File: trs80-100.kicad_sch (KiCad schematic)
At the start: 120 parts, among them CN2 A-7224, CN3 TCS-4480, CN4 TCS-4490, CN6 RS232C, J1 Adapter Jack CN9, M27 4011, M28 4013, SW3 SLB-22BP-03, SW4 Reset Switch, SW5 SSP32201, T10 2SC2603, T11 2SC2603, T13 2SC2603(E), T14 2SC2603(E), T15 2SC2603(E), T16 2SC2603(E), T17 2SC2603(E), T18 2SC2603, T19 2SA1115, T20 2SC2603, T21 2SC2603(E), T22 2SC2603(E), T25 2SC2603, T27 2SC2603, T28 2SA1115, T9 2SC2603

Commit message: Progress BCR, CMT section.
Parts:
- added C63: 100n, symbol Device:C
- added C64, C67: 47n, symbol Device:C
- added D17, D5, D6, D7: 1S2076, symbol Device:D
- added M30: TL064, symbol Amplifier_Operational:TL064
- added M34: 4584, symbol trs80-100:4584
- added R131, R52: 1k, symbol Device:R
- added R132: 150k, symbol Device:R
- added R136, R93: 68k, symbol Device:R
- added R50, R55: 3.3k, symbol Device:R
- added R51: 2.2k, symbol Device:R
- added R53: 100k, symbol Device:R
- added R54: 12k, symbol Device:R
- added R62, R67, R71, R72: 33k, symbol Device:R
- added R95: 100, symbol Device:R
- added RY1: FBR211CD005-M, symbol trs80-100:FBR211CD005-M
- added T6: 2SC2603, Package_TO_SOT_THT:TO-92_Inline, symbol Transistor_BJT:2N3904
- renumbered R52 to R152, Rqq to R999
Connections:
- net GNDPWR: now also C64.1, C67.2, D5.2 (A), D6.1 (K), D7.2 (A), M34.7 (GND), R131.2, R53.2, R55.2, R93.2, T6.1 (E)
- net VDD: now also C67.1, M30.4 (V+), M34.14 (VCC), R136.1, R62.2, R67.2, R71.2
- net VEE: now also M30.11 (V-)
- net VR: now also D17.1 (K), RY1.5
- net at CN2.2 (RxD), R70.1: now also M34.9
- net at CN3.1 (REM1): now also RY1.4
- net at CN3.3 (REM2): now also RY1.6
- net at CN3.4 (RxC): now also R95.1
- net at CN3.5 (TxC): now also R54.1, R55.1
- new net: M30.10 (+), R131.1, R132.1, R136.2
- new net: M30.8, R132.2, R72.1
- new net: D5.1 (K), D6.2 (A), R52.1, R53.1, R95.2
- new net: R50.1, R93.1, T6.2 (B)
- new net: M34.4, R50.2
- new net: C63.2, M34.12, R71.1
- new net: D7.1 (K), M34.11, R72.2
- new net: M30.9 (-), R52.2
- new net: D17.2 (A), RY1.2, T6.3 (C)
- new net: C64.2, R51.1, R54.2
- new net: C63.1, R51.2
- new net: M34.10, R62.1
- new net ~{REMOTE}: M34.3, R67.1
- no-connect marks 1 -> 8
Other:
- moved on the sheet: CN3, CN4

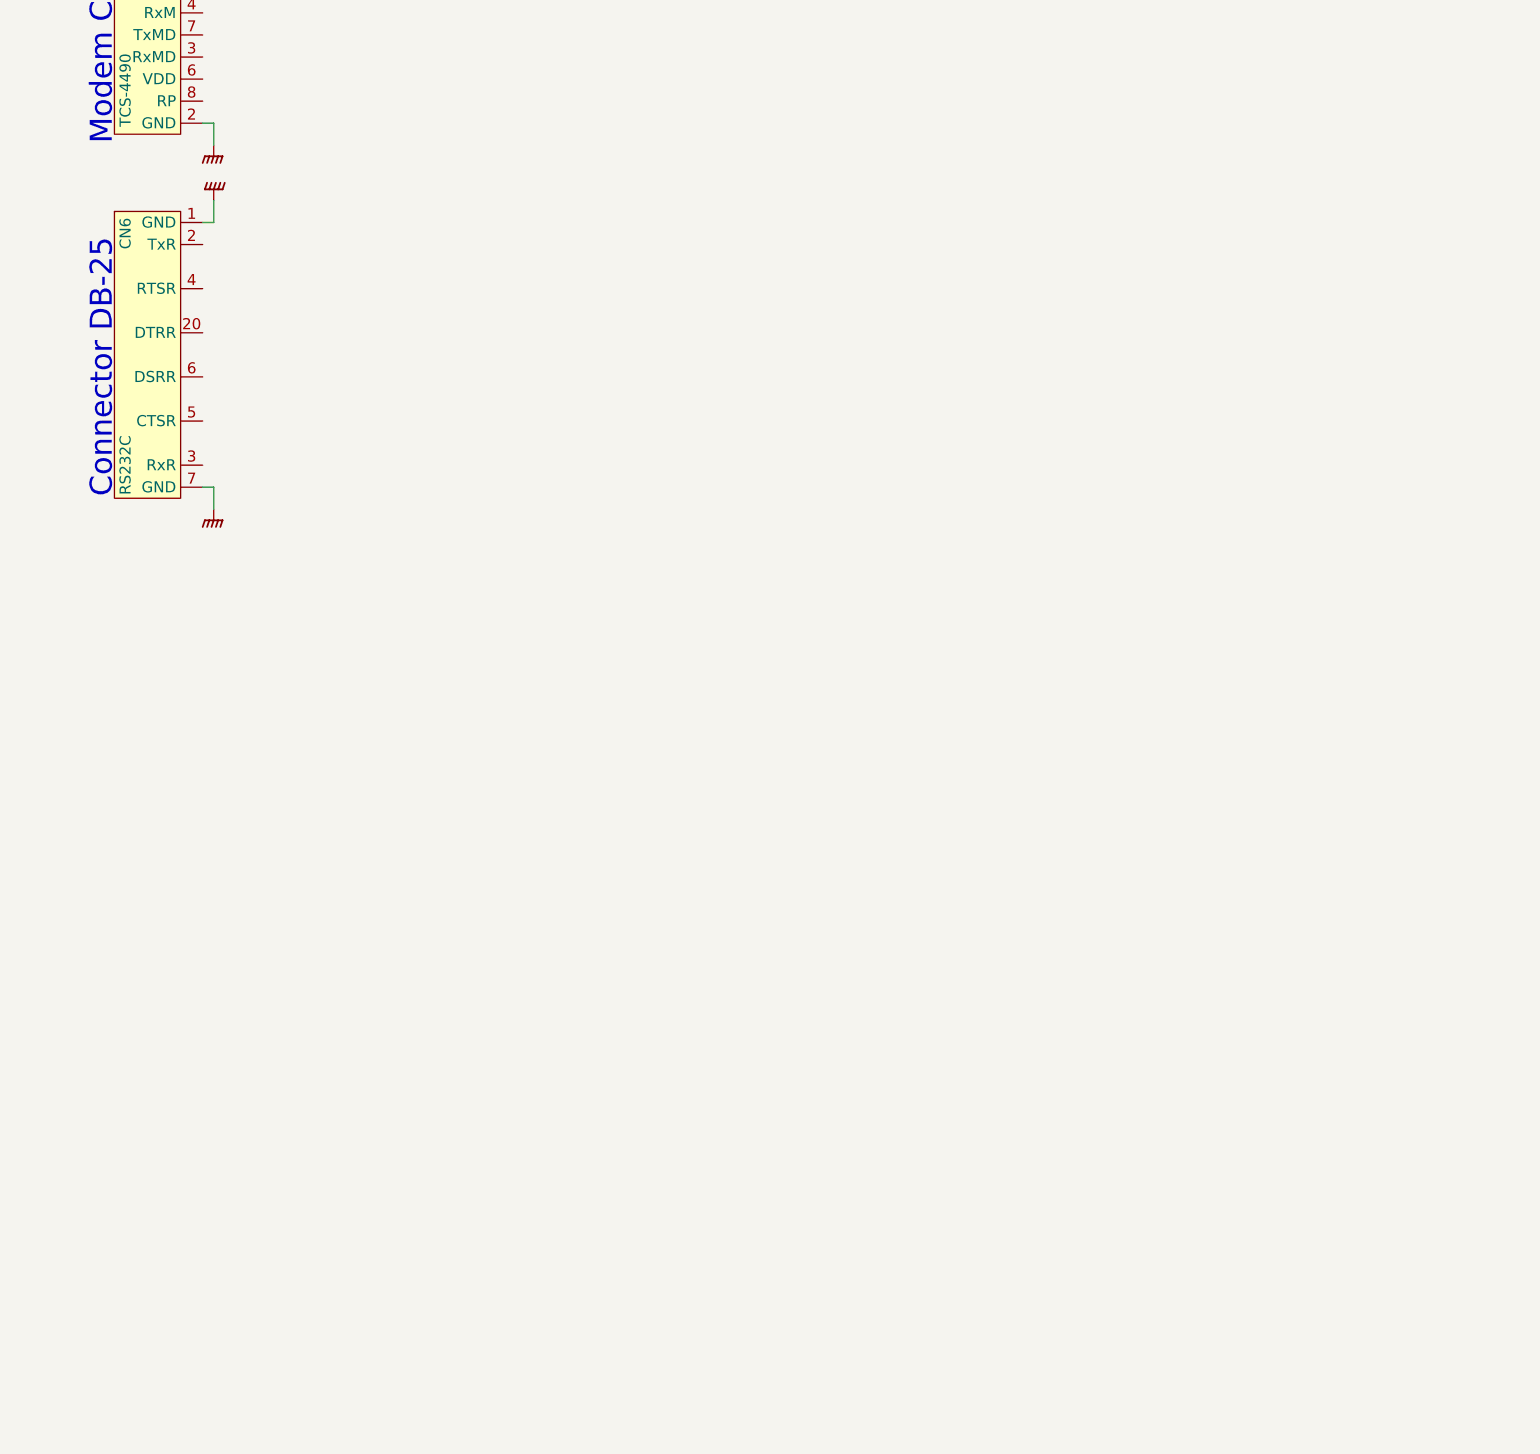
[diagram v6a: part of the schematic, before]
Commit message: Progress RS232 interface.
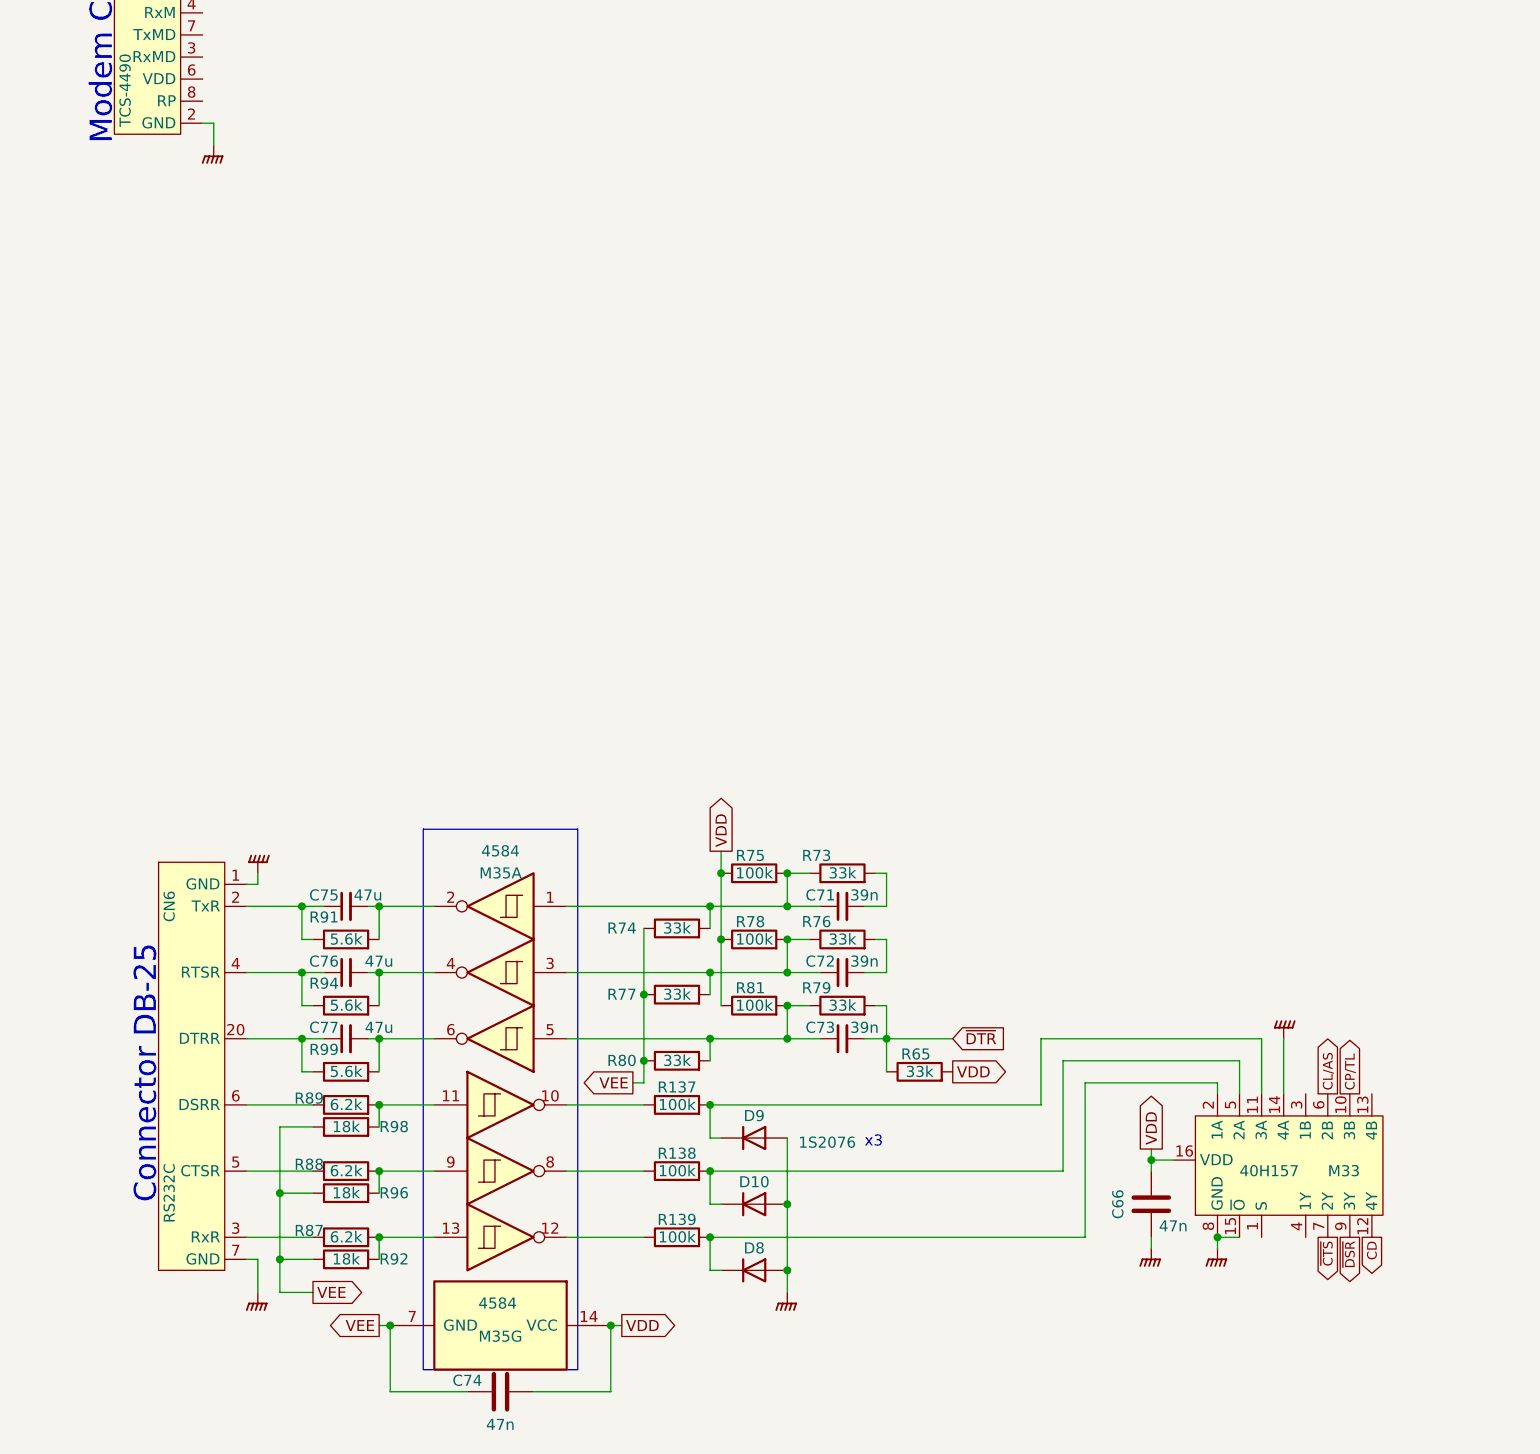
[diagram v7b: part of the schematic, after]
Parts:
- added C66, C74: 47n, symbol Device:C
- added C71, C72, C73: 39n, symbol Device:C_Small
- added C75, C76, C77: 47u, symbol Device:C_Small
- added D10, D8, D9: 1S2076, symbol Device:D
- added M33: 40H157, symbol trs80-100:40H157
- added M35: 4584, symbol trs80-100:4584
- added R137, R138, R139, R75, R78, R81: 100k, symbol Device:R
- added R65, R73, R74, R76, R77, R79, R80: 33k, symbol Device:R
- added R87, R88, R89: 6.2k, symbol Device:R
- added R91, R94, R99: 5.6k, symbol Device:R
- added R92, R96, R98: 18k, symbol Device:R
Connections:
- net GNDPWR: now also C66.2, D10.2 (A), D8.2 (A), D9.2 (A), M33.14 (4A), M33.15 (~{O}), M33.8 (GND)
- net VDD: now also C66.1, C74.1, M33.16 (VDD), M35.14 (VCC), R65.2, R75.1, R78.1, R81.1
- net VEE: now also C74.2, M35.7 (GND), R74.1, R77.1, R80.1, R92.1, R96.1, R98.1
- net at CN6.2 (TxR): now also C75.1, R91.1
- net at CN6.20 (DTRR): now also C77.1, R99.1
- net at CN6.3 (RxR): now also R87.1
- net at CN6.4 (RTSR): now also C76.1, R94.1
- net at CN6.5 (CTSR): now also R88.1
- net at CN6.6 (DSRR): now also R89.1
- new net: M35.11, R89.2, R98.2
- new net: C73.1, M35.5, R79.1, R80.2, R81.2
- new net: C71.1, M35.1, R73.1, R74.2, R75.2
- new net: C72.1, M35.3, R76.1, R77.2, R78.2
- new net: C75.2, M35.2, R91.2
- new net: C71.2, R73.2
- new net: D10.1 (K), M33.5 (2A), R138.2
- new net: C76.2, M35.4, R94.2
- new net: C72.2, R76.2
- new net: C77.2, M35.6, R99.2
- new net: M35.10, R137.1
- new net: D9.1 (K), M33.11 (3A), R137.2
- new net: M35.9, R88.2, R96.2
- new net: M35.8, R138.1
- new net: D8.1 (K), M33.2 (1A), R139.2
- new net: M35.13, R87.2, R92.2
- new net: M35.12, R139.1
- new net CD: M33.12 (4Y)
- new net CL/AS: M33.6 (2B)
- new net CP/TL: M33.10 (3B)
- new net ~{CTS}: M33.7 (2Y)
- new net ~{DSR}: M33.9 (3Y)
- new net ~{DTR}: C73.2, R65.1, R79.2
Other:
- moved on the sheet: CN6

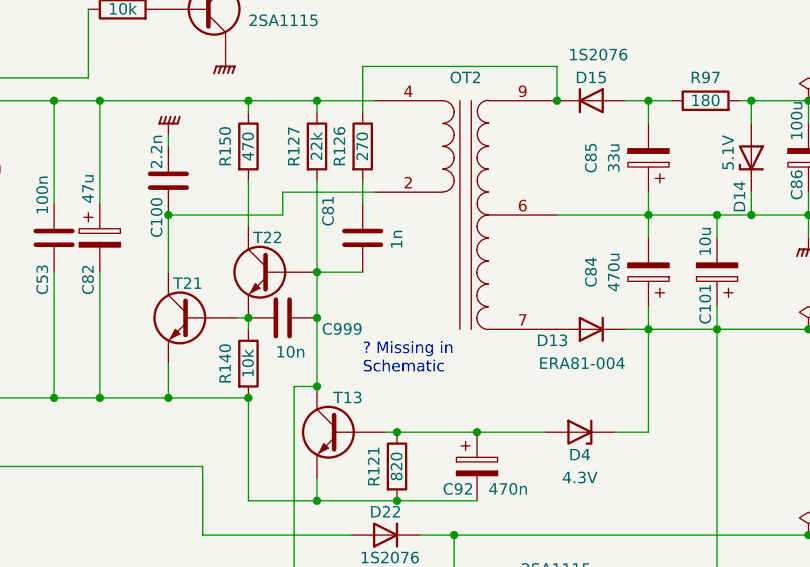
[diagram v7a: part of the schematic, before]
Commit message: Mystery capacitor is likely C104 - the only one with value 10nF
... or 10000pF as they liked to call it back in the day.
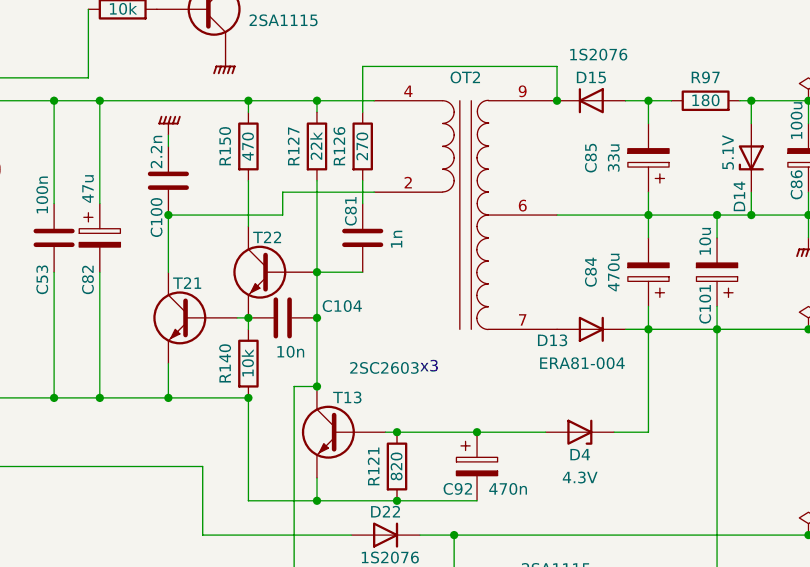
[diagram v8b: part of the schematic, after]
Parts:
- T13: value 2SC2603(E) -> 2SC2603
- renumbered C999 to C104
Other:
- note removed: "? Missing in Schematic"
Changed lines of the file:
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@@
     (stroke (width 0) (type default) (color 0 0 0 0))
   )
+  (text "x3" (at 193.04 66.04 0)
+    (effects (font (size 1.27 1.27)) (justify left bottom))
+  )
   (text "Low Battery" (at 191.77 17.78 0)
     (effects (font (size 1.27 1.27)) (justify left bottom))
@@
     (effects (font (size 1.27 1.27)) (justify left bottom))
   )
-  (text "? Missing in\nSchematic" (at 186.69 66.04 0)
-    (effects (font (size 1.27 1.27)) (justify left bottom))
-  )
   (text "x2" (at 19.05 36.83 90)
     (effects (font (size 1.27 1.27)) (justify left bottom))
@@
   (symbol (lib_id "Device:C") (at 186.69 50.8 0) (unit 1)
     (in_bom yes) (on_board yes)
-    (property "Reference" "C81" (id 0) (at 182.88 49.53 90)
+    (property "Reference" "C81" (id 0) (at 185.42 49.53 90)
       (effects (font (size 1.27 1.27)) (justify left))
     )
@@
   (symbol (lib_id "Device:C") (at 177.8 59.69 90) (unit 1)
     (in_bom yes) (on_board yes)
-    (property "Reference" "C999" (id 0) (at 186.69 60.96 90)
+    (property "Reference" "C104" (id 0) (at 186.69 58.42 90)
       (effects (font (size 1.27 1.27)) (justify left))
     )
@@
       (effects (font (size 1.27 1.27)) (justify left))
     )
-    (property "Value" "2SC2603(E)" (id 1) (at 180.34 74.93 0)
-      (effects (font (size 1.27 1.27)) (justify left) hide)
+    (property "Value" "2SC2603" (id 1) (at 193.04 66.04 0)
+      (effects (font (size 1.27 1.27)) (justify left bottom))
     )
     (property "Footprint" "Package_TO_SOT_THT:TO-92_Inline" (id 2) (at 179.07 74.295 0)
@@
       (reference "C101") (unit 1) (value "10u") (footprint "")
     )
+    (path "/610ba8e7-71d1-4ade-8e2e-f4d68d6e4ea2"
+      (reference "C104") (unit 1) (value "10n") (footprint "")
+    )
     (path "/83e61065-233d-4330-b7a4-41423bd3515a"
       (reference "C107") (unit 1) (value "270p") (footprint "")
@@
       (reference "C111") (unit 1) (value "3.3n") (footprint "")
     )
-    (path "/610ba8e7-71d1-4ade-8e2e-f4d68d6e4ea2"
-      (reference "C999") (unit 1) (value "10n") (footprint "")
-    )
     (path "/602e5280-8c4b-44d4-917a-a7ccb81b1695"
       (reference "CN2") (unit 1) (value "A-7224") (footprint "")
@@
     )
     (path "/c334d95e-8e5b-4452-8d89-6aeff14a6163"
-      (reference "T13") (unit 1) (value "2SC2603(E)") (footprint "Package_TO_SOT_THT:TO-92_Inline")
+      (reference "T13") (unit 1) (value "2SC2603") (footprint "Package_TO_SOT_THT:TO-92_Inline")
     )
     (path "/75dc4e27-5564-4b18-b662-1d9cc22edfcb"
